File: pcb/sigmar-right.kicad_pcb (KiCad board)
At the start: 2 copper layers, 137.2 x 101.7 mm, 77 parts, among them J1 AudioJack4, J2 AVR-ISP-6, SW1 Cherry-MX-LED-APA102, SW10 Cherry-MX-LED-APA102, SW11 Cherry-MX-LED-APA102, SW12 Cherry-MX-LED-APA102, SW13 Cherry-MX-LED-APA102, SW14 Cherry-MX-LED-APA102, SW15 Cherry-MX-LED-APA102, SW16 Cherry-MX-LED-APA102, SW17 Cherry-MX-LED-APA102, SW18 Cherry-MX-LED-APA102, SW19 Cherry-MX-LED-APA102, SW2 Cherry-MX-LED-APA102, SW20 Cherry-MX-LED-APA102, SW21 Cherry-MX-LED-APA102, SW22 Cherry-MX-LED-APA102, SW23 Cherry-MX-LED-APA102, SW24 Cherry-MX-LED-APA102, SW25 Cherry-MX-LED-APA102, SW26 SW_Push, SW3 Cherry-MX-LED-APA102, SW4 Cherry-MX-LED-APA102, SW5 Cherry-MX-LED-APA102, SW6 Cherry-MX-LED-APA102, SW7 Cherry-MX-LED-APA102, SW8 Cherry-MX-LED-APA102, SW9 Cherry-MX-LED-APA102, U1 ATmega32U4-AU, Y1 16MHz

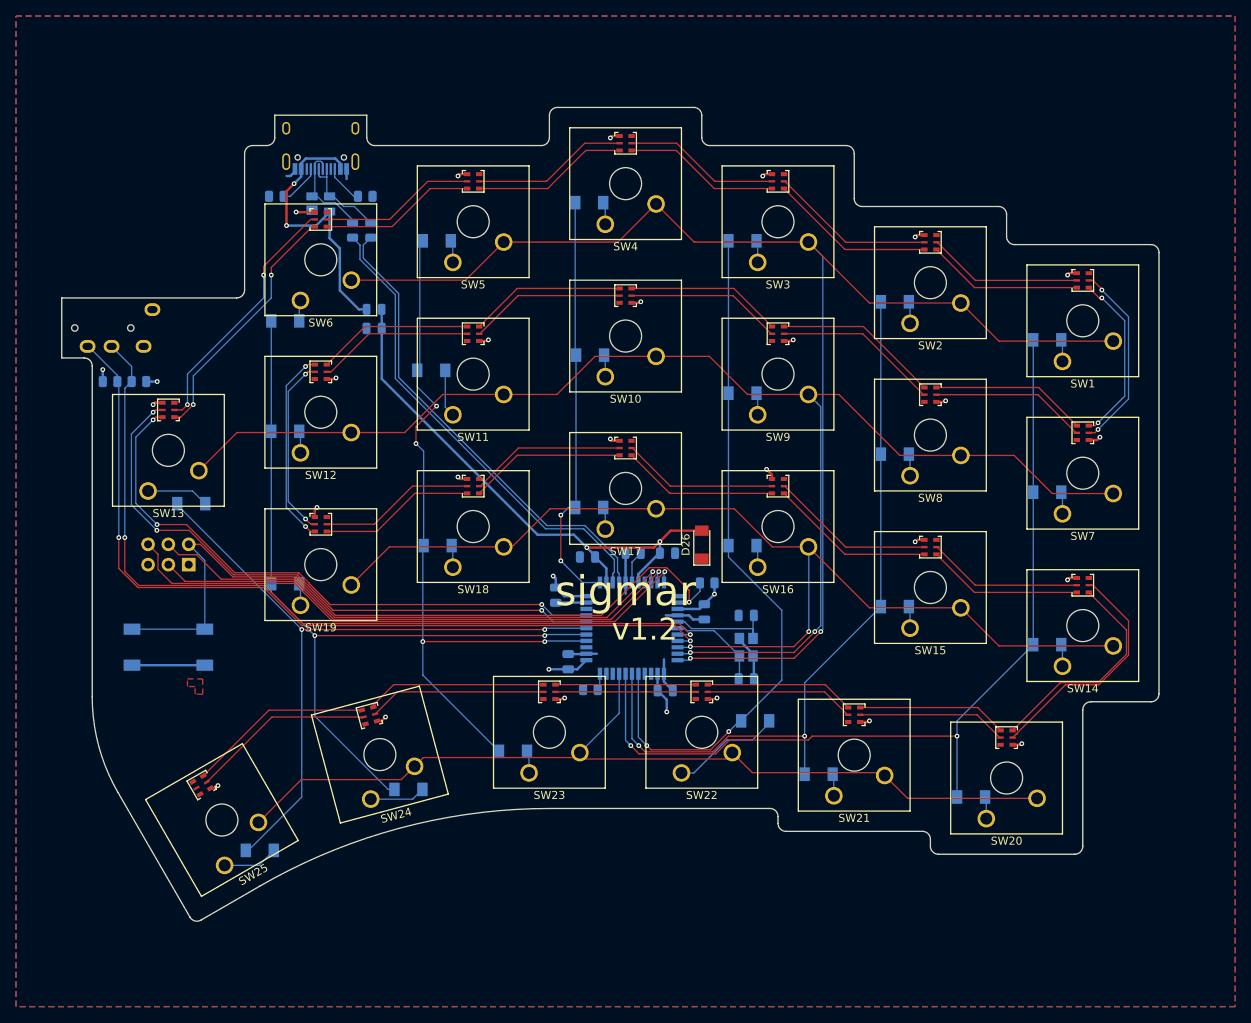
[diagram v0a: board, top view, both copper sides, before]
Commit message: make room for stabilizers
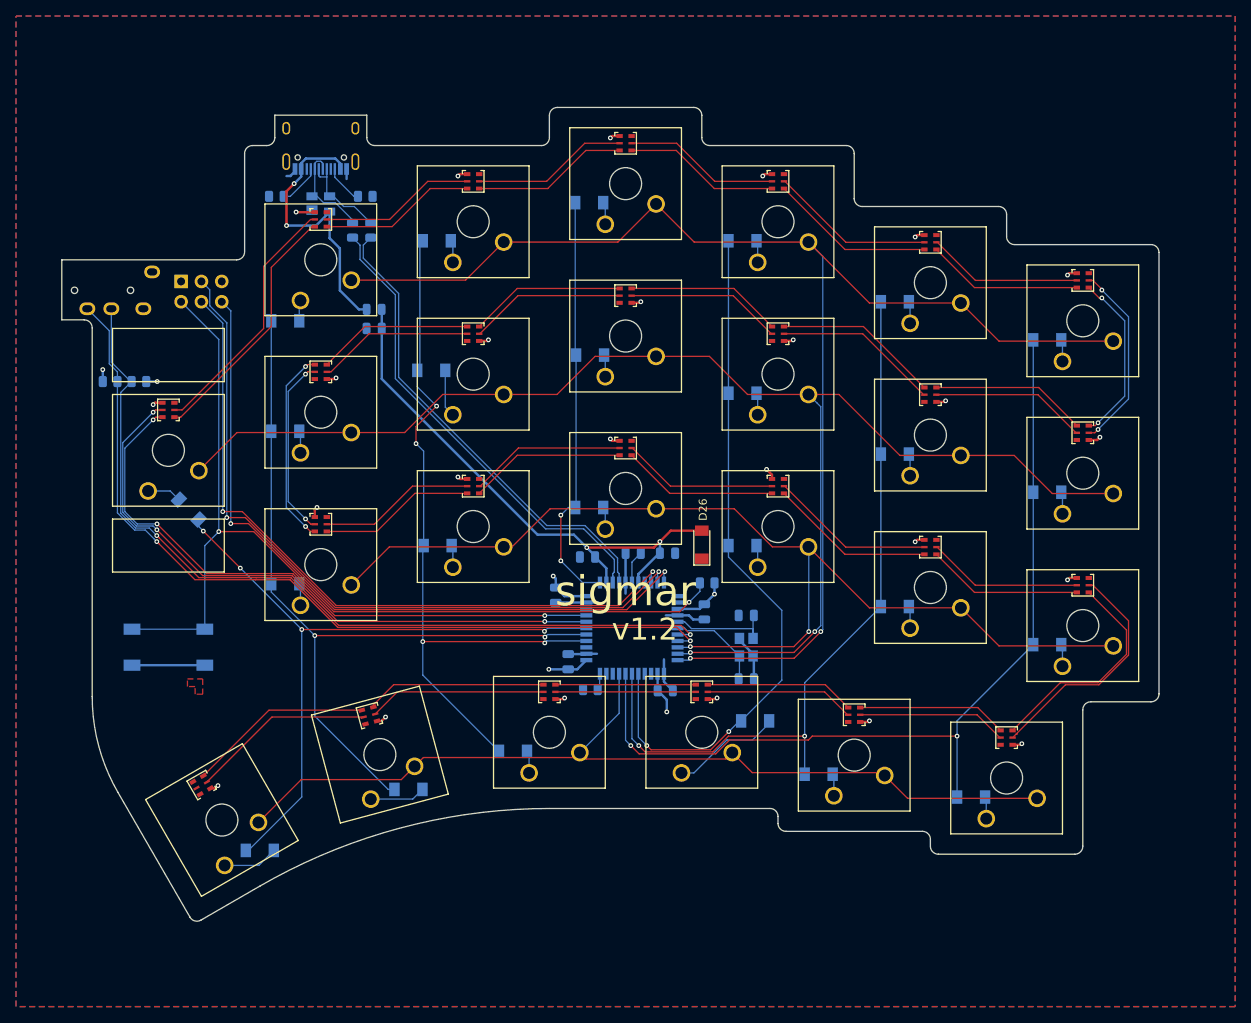
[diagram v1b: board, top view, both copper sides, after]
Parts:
- J2: value AVR-ISP-6 -> Reset_Pretty-Mask
- moved J2 33.1 mm to (102.3, 67.3), turned to 90 degrees
- moved J1 4.71 mm to (84.8, 67.2)
- moved D13 0.80 mm to (100.7, 94.6), turned to 315 degrees
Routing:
- net /MOSI: track 68.1 -> 92.8 mm, vias 1 -> 2
- net /RESET: track 96.3 -> 120.5 mm, vias 1 -> 2
- net /SCK: track 68.2 -> 89.2 mm, vias 1 -> 2
- net /MISO: track 73.7 -> 90.3 mm, vias 1 -> 2
- net Net-(D13-Pad1): track 7.81 -> 4.46 mm
- net /COL7: track 88.5 -> 85.6 mm, vias 2 -> 4
- net /LED_SDI: track 74.8 -> 77.3 mm
- net /LED_CKI: track 76.9 -> 79.0 mm
- net /SCL: track 105.1 -> 106.3 mm
- net /SDA: track 106.3 -> 106.9 mm
- net Net-(SW13-Pad7): vias 2 -> 0
- net Net-(SW13-Pad6): vias 2 -> 0
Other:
- outline, holes or cut-outs redrawn
